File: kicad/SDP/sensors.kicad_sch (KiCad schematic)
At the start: 13 parts, among them J10 Limit, J11 Conn_01x07, J12 Conn_01x07, J13 Conn_01x03, J14 Conn_01x03, J8 Conn_01x07, J9 Conn_01x07

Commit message: PCB layout and schematic updates
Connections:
- removed net P93_LIMIT: J10.1 (Pin_1), J10.11 (Pin_11), J10.3 (Pin_3), J10.5 (Pin_5), J10.7 (Pin_7), J10.9 (Pin_9), R20.2, R21.2, R22.2, R23.2, R24.2, R25.2
- new net P100_LIMIT: J10.1 (Pin_1), R20.2
- new net P95_LIMIT: J10.11 (Pin_11), R25.2
- new net P96_LIMIT: J10.9 (Pin_9), R24.2
- new net P97_LIMIT: J10.7 (Pin_7), R23.2
- new net P98_LIMIT: J10.5 (Pin_5), R22.2
- new net P99_LIMIT: J10.3 (Pin_3), R21.2
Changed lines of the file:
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@@
     (effects (font (size 1.27 1.27)) (justify left bottom))
+  )
+  (global_label "P100_LIMIT" (shape input) (at 179.832 53.086 180) (fields_autoplaced)
+    (effects (font (size 1.27 1.27)) (justify right))
+    (property "Intersheet References" "${INTERSHEET_REFS}" (id 0) (at 166.896 53.1654 0)
+      (effects (font (size 1.27 1.27)) (justify right) hide)
+    )
   )
   (global_label "P57_SCL1" (shape input) (at 91.694 39.116 180) (fields_autoplaced)
@@
     (effects (font (size 1.27 1.27)) (justify right))
     (property "Intersheet References" "${INTERSHEET_REFS}" (id 0) (at 73.3757 44.1166 0)
-      (effects (font (size 1.27 1.27)) (justify right) hide)
-    )
-  )
-  (global_label "P93_LIMIT" (shape input) (at 179.832 60.706 180) (fields_autoplaced)
-    (effects (font (size 1.27 1.27)) (justify right))
-    (property "Intersheet References" "${INTERSHEET_REFS}" (id 0) (at 168.1056 60.6266 0)
       (effects (font (size 1.27 1.27)) (justify right) hide)
     )
@@
     )
   )
+  (global_label "P95_LIMIT" (shape input) (at 179.832 65.786 180) (fields_autoplaced)
+    (effects (font (size 1.27 1.27)) (justify right))
+    (property "Intersheet References" "${INTERSHEET_REFS}" (id 0) (at 168.1056 65.7066 0)
+      (effects (font (size 1.27 1.27)) (justify right) hide)
+    )
+  )
   (global_label "P56_SDA1" (shape input) (at 91.694 36.576 180) (fields_autoplaced)
     (effects (font (size 1.27 1.27)) (justify right))
     (property "Intersheet References" "${INTERSHEET_REFS}" (id 0) (at 79.8466 36.4966 0)
+      (effects (font (size 1.27 1.27)) (justify right) hide)
+    )
+  )
+  (global_label "P97_LIMIT" (shape input) (at 179.832 60.706 180) (fields_autoplaced)
+    (effects (font (size 1.27 1.27)) (justify right))
+    (property "Intersheet References" "${INTERSHEET_REFS}" (id 0) (at 168.1056 60.6266 0)
       (effects (font (size 1.27 1.27)) (justify right) hide)
     )
@@
     )
   )
-  (global_label "P93_LIMIT" (shape input) (at 179.832 63.246 180) (fields_autoplaced)
+  (global_label "P96_LIMIT" (shape input) (at 179.832 63.246 180) (fields_autoplaced)
     (effects (font (size 1.27 1.27)) (justify right))
     (property "Intersheet References" "${INTERSHEET_REFS}" (id 0) (at 168.1056 63.1666 0)
+      (effects (font (size 1.27 1.27)) (justify right) hide)
+    )
+  )
+  (global_label "P99_LIMIT" (shape input) (at 179.832 55.626 180) (fields_autoplaced)
+    (effects (font (size 1.27 1.27)) (justify right))
+    (property "Intersheet References" "${INTERSHEET_REFS}" (id 0) (at 168.1056 55.7054 0)
       (effects (font (size 1.27 1.27)) (justify right) hide)
     )
@@
     )
   )
+  (global_label "P98_LIMIT" (shape input) (at 179.832 58.166 180) (fields_autoplaced)
+    (effects (font (size 1.27 1.27)) (justify right))
+    (property "Intersheet References" "${INTERSHEET_REFS}" (id 0) (at 168.1056 58.2454 0)
+      (effects (font (size 1.27 1.27)) (justify right) hide)
+    )
+  )
   (global_label "P57_SCL1" (shape input) (at 91.694 72.39 180) (fields_autoplaced)
     (effects (font (size 1.27 1.27)) (justify right))
     (property "Intersheet References" "${INTERSHEET_REFS}" (id 0) (at 79.9071 72.3106 0)
-      (effects (font (size 1.27 1.27)) (justify right) hide)
-    )
-  )
-  (global_label "P93_LIMIT" (shape input) (at 179.832 58.166 180) (fields_autoplaced)
-    (effects (font (size 1.27 1.27)) (justify right))
-    (property "Intersheet References" "${INTERSHEET_REFS}" (id 0) (at 168.1056 58.0866 0)
-      (effects (font (size 1.27 1.27)) (justify right) hide)
-    )
-  )
-  (global_label "P93_LIMIT" (shape input) (at 179.832 55.626 180) (fields_autoplaced)
-    (effects (font (size 1.27 1.27)) (justify right))
-    (property "Intersheet References" "${INTERSHEET_REFS}" (id 0) (at 168.1056 55.5466 0)
       (effects (font (size 1.27 1.27)) (justify right) hide)
     )
@@
       (effects (font (size 1.27 1.27)) (justify right) hide)
     )
-  )
-  (global_label "P93_LIMIT" (shape input) (at 179.832 65.786 180) (fields_autoplaced)
-    (effects (font (size 1.27 1.27)) (justify right))
-    (property "Intersheet References" "${INTERSHEET_REFS}" (id 0) (at 168.1056 65.7066 0)
-      (effects (font (size 1.27 1.27)) (justify right) hide)
-    )
-  )
-  (global_label "P93_LIMIT" (shape input) (at 179.832 53.086 180) (fields_autoplaced)
-    (effects (font (size 1.27 1.27)) (justify right))
-    (property "Intersheet References" "${INTERSHEET_REFS}" (id 0) (at 168.1056 53.0066 0)
-      (effects (font (size 1.27 1.27)) (justify right) hide)
-    )

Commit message: Controller PCB layout
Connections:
- net P33_TOF2_CE renamed P34_TOF2_CE
- net P34_TOF3_CE renamed P41_TOF3_CE
- net P35_TOF4_CE renamed P43_TOF4_CE
- net P41_TOF1_GPIO1 renamed P33_TOF1_GPIO1
- net P42_TOF2_GPIO1 renamed P35_TOF2_GPIO1
- net P43_TOF3_GPIO1 renamed P42_TOF3_GPIO1
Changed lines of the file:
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@@
     )
   )
-  (global_label "P42_TOF2_GPIO1" (shape input) (at 91.694 44.196 180) (fields_autoplaced)
+  (global_label "P35_TOF2_GPIO1" (shape input) (at 91.694 44.196 180) (fields_autoplaced)
     (effects (font (size 1.27 1.27)) (justify right))
     (property "Intersheet References" "${INTERSHEET_REFS}" (id 0) (at 73.3757 44.1166 0)
@@
     )
   )
-  (global_label "P34_TOF3_CE" (shape input) (at 40.894 74.93 180) (fields_autoplaced)
+  (global_label "P41_TOF3_CE" (shape input) (at 40.894 74.93 180) (fields_autoplaced)
     (effects (font (size 1.27 1.27)) (justify right))
     (property "Intersheet References" "${INTERSHEET_REFS}" (id 0) (at 25.8414 74.8506 0)
@@
     )
   )
-  (global_label "P43_TOF3_GPIO1" (shape input) (at 40.894 77.47 180) (fields_autoplaced)
+  (global_label "P42_TOF3_GPIO1" (shape input) (at 40.894 77.47 180) (fields_autoplaced)
     (effects (font (size 1.27 1.27)) (justify right))
     (property "Intersheet References" "${INTERSHEET_REFS}" (id 0) (at 22.5757 77.3906 0)
@@
     )
   )
-  (global_label "P35_TOF4_CE" (shape input) (at 91.694 74.93 180) (fields_autoplaced)
+  (global_label "P43_TOF4_CE" (shape input) (at 91.694 74.93 180) (fields_autoplaced)
     (effects (font (size 1.27 1.27)) (justify right))
     (property "Intersheet References" "${INTERSHEET_REFS}" (id 0) (at 76.6414 74.8506 0)
@@
     )
   )
-  (global_label "P41_TOF1_GPIO1" (shape input) (at 39.624 44.45 180) (fields_autoplaced)
+  (global_label "P33_TOF1_GPIO1" (shape input) (at 39.624 44.45 180) (fields_autoplaced)
     (effects (font (size 1.27 1.27)) (justify right))
     (property "Intersheet References" "${INTERSHEET_REFS}" (id 0) (at 21.3057 44.3706 0)
@@
     )
   )
-  (global_label "P33_TOF2_CE" (shape input) (at 91.694 41.656 180) (fields_autoplaced)
+  (global_label "P34_TOF2_CE" (shape input) (at 91.694 41.656 180) (fields_autoplaced)
     (effects (font (size 1.27 1.27)) (justify right))
     (property "Intersheet References" "${INTERSHEET_REFS}" (id 0) (at 76.6414 41.5766 0)

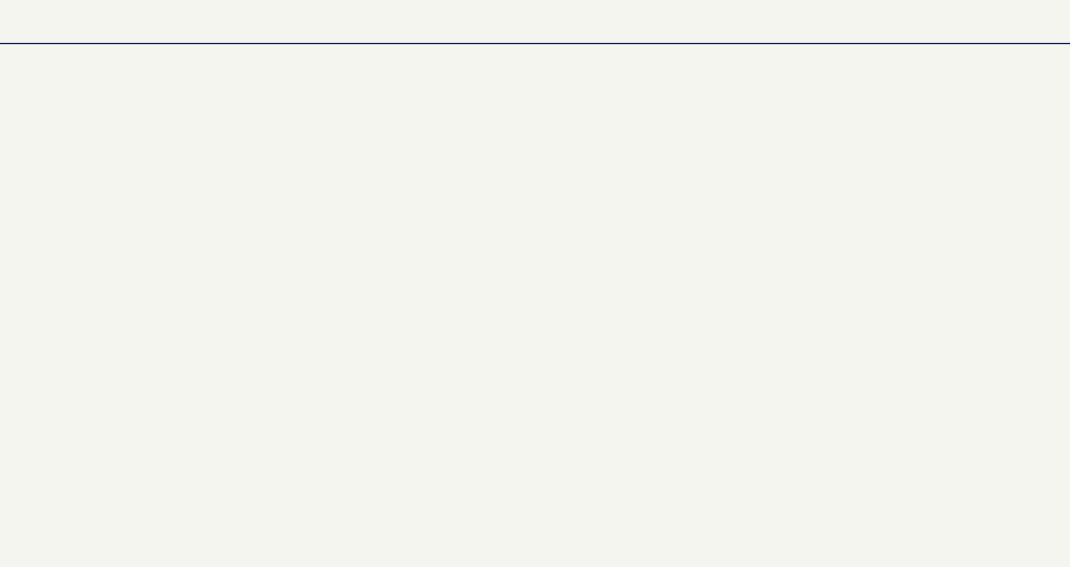
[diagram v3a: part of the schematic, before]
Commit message: Added proximity sensor headers
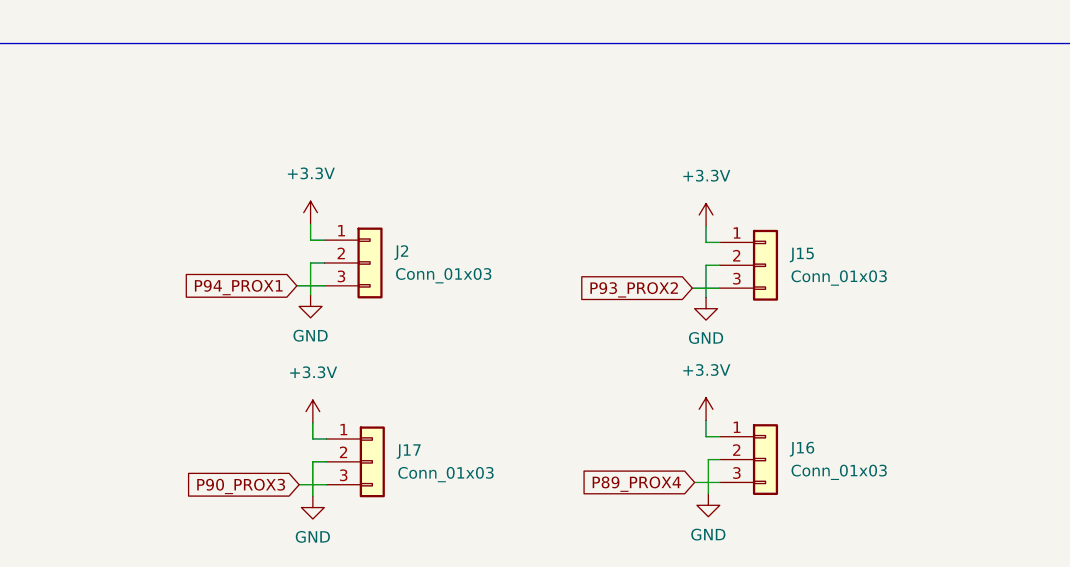
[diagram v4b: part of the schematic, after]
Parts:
- added J15, J16, J17, J2: Conn_01x03, Connector_PinSocket_2.54mm:PinSocket_1x03_P2.54mm_Vertical, symbol Connector_Generic:Conn_01x03
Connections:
- net +3V3: now also J15.1 (Pin_1), J16.1 (Pin_1), J17.1 (Pin_1), J2.1 (Pin_1)
- net GND: now also J15.2 (Pin_2), J16.2 (Pin_2), J17.2 (Pin_2), J2.2 (Pin_2)
- new net P89_PROX4: J16.3 (Pin_3)
- new net P90_PROX3: J17.3 (Pin_3)
- new net P93_PROX2: J15.3 (Pin_3)
- new net P94_PROX1: J2.3 (Pin_3)

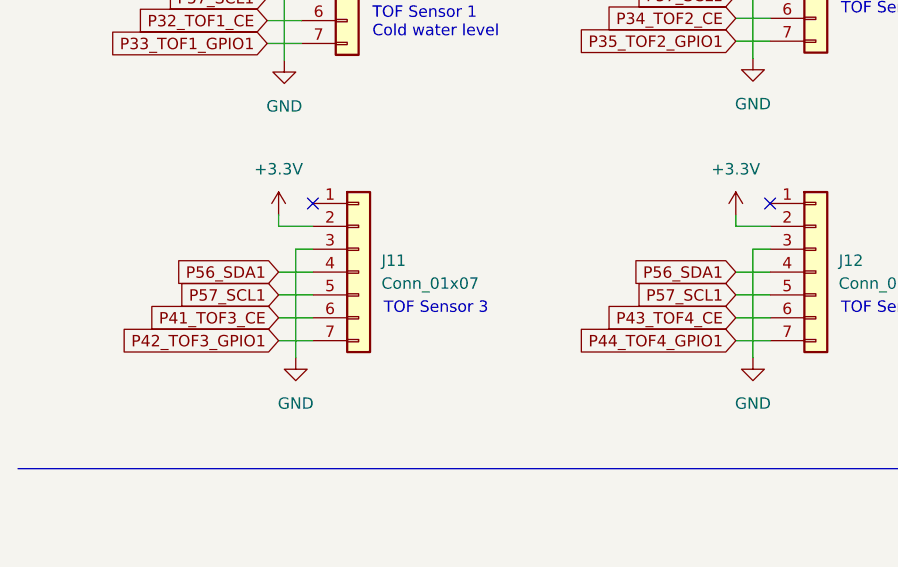
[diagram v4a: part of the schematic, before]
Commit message: Controller and motor PCB silkscreen and final layout
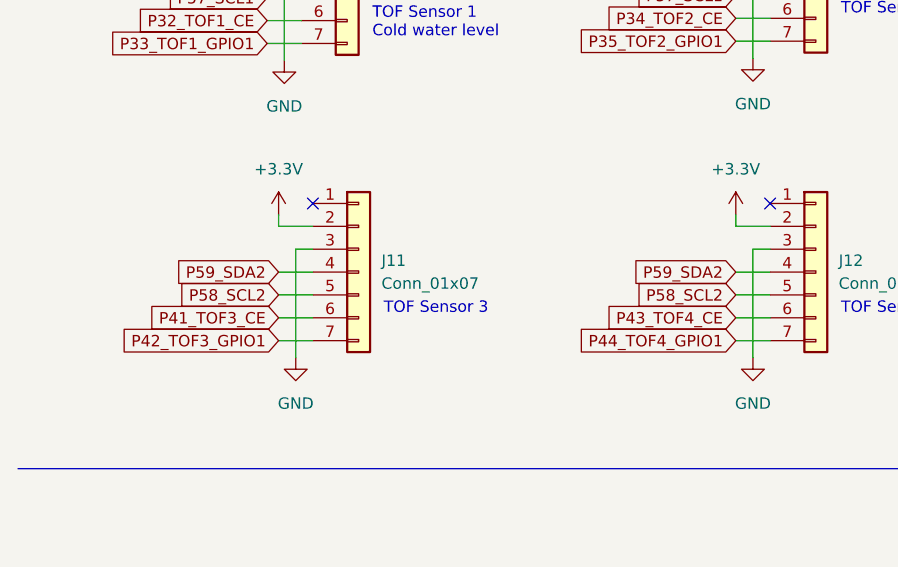
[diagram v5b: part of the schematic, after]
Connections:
- net P56_SDA1: no longer J11.4 (Pin_4), J12.4 (Pin_4)
- net P57_SCL1: no longer J11.5 (Pin_5), J12.5 (Pin_5)
- new net P58_SCL2: J11.5 (Pin_5), J12.5 (Pin_5)
- new net P59_SDA2: J11.4 (Pin_4), J12.4 (Pin_4)
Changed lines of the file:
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@@
+    )
+  )
+  (global_label "P58_SCL2" (shape input) (at 91.694 72.39 180) (fields_autoplaced)
+    (effects (font (size 1.27 1.27)) (justify right))
+    (property "Intersheet References" "${INTERSHEET_REFS}" (id 0) (at 79.9071 72.4694 0)
+      (effects (font (size 1.27 1.27)) (justify right) hide)
     )
   )
@@
     (effects (font (size 1.27 1.27)) (justify right))
     (property "Intersheet References" "${INTERSHEET_REFS}" (id 0) (at 27.7766 36.7506 0)
-      (effects (font (size 1.27 1.27)) (justify right) hide)
-    )
-  )
-  (global_label "P56_SDA1" (shape input) (at 40.894 69.85 180) (fields_autoplaced)
-    (effects (font (size 1.27 1.27)) (justify right))
-    (property "Intersheet References" "${INTERSHEET_REFS}" (id 0) (at 29.0466 69.7706 0)
-      (effects (font (size 1.27 1.27)) (justify right) hide)
-    )
-  )
-  (global_label "P56_SDA1" (shape input) (at 91.694 69.85 180) (fields_autoplaced)
-    (effects (font (size 1.27 1.27)) (justify right))
-    (property "Intersheet References" "${INTERSHEET_REFS}" (id 0) (at 79.8466 69.7706 0)
       (effects (font (size 1.27 1.27)) (justify right) hide)
     )
@@
     )
   )
-  (global_label "P57_SCL1" (shape input) (at 40.894 72.39 180) (fields_autoplaced)
+  (global_label "P59_SDA2" (shape input) (at 91.694 69.85 180) (fields_autoplaced)
     (effects (font (size 1.27 1.27)) (justify right))
-    (property "Intersheet References" "${INTERSHEET_REFS}" (id 0) (at 29.1071 72.3106 0)
+    (property "Intersheet References" "${INTERSHEET_REFS}" (id 0) (at 79.8466 69.9294 0)
       (effects (font (size 1.27 1.27)) (justify right) hide)
     )
@@
     (effects (font (size 1.27 1.27)) (justify right))
     (property "Intersheet References" "${INTERSHEET_REFS}" (id 0) (at 21.6806 120.0626 0)
+      (effects (font (size 1.27 1.27)) (justify right) hide)
+    )
+  )
+  (global_label "P59_SDA2" (shape input) (at 40.894 69.85 180) (fields_autoplaced)
+    (effects (font (size 1.27 1.27)) (justify right))
+    (property "Intersheet References" "${INTERSHEET_REFS}" (id 0) (at 29.0466 69.9294 0)
       (effects (font (size 1.27 1.27)) (justify right) hide)
     )
@@
     )
   )
+  (global_label "P58_SCL2" (shape input) (at 40.894 72.39 180) (fields_autoplaced)
+    (effects (font (size 1.27 1.27)) (justify right))
+    (property "Intersheet References" "${INTERSHEET_REFS}" (id 0) (at 29.1071 72.4694 0)
+      (effects (font (size 1.27 1.27)) (justify right) hide)
+    )
+  )
   (global_label "P98_LIMIT" (shape input) (at 179.832 58.166 180) (fields_autoplaced)
     (effects (font (size 1.27 1.27)) (justify right))
@@
       (effects (font (size 1.27 1.27)) (justify right) hide)
     )
-  )
-  (global_label "P57_SCL1" (shape input) (at 91.694 72.39 180) (fields_autoplaced)
-    (effects (font (size 1.27 1.27)) (justify right))
-    (property "Intersheet References" "${INTERSHEET_REFS}" (id 0) (at 79.9071 72.3106 0)
-      (effects (font (size 1.27 1.27)) (justify right) hide)
-    )
